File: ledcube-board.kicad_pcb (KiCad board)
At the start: 4 copper layers, 181 parts, among them J1 Conn_01x02, J10 molex_53261-0871, J11 104031-0811, J12 molex_53261-0871, J2 molex_53261-0871, J3 molex_53261-0871, J4 molex_53261-0871, J5 molex_53261-0871, J6 molex_53261-0871, J7 molex_53261-0871, J8 molex_53261-0871, J9 molex_53261-0871, Q1 Q_NMOS_GDSD, Q2 Q_NMOS_GDSD, Q3 Q_NMOS_GDSD, Q4 Q_NMOS_GDSD, Q5 Q_NMOS_GDSD, Q6 Q_NMOS_GDSD, Q7 Q_NMOS_GDSD, Q8 Q_NMOS_GDSD, U1 LM1085IS-12, U10 ESP32-DEVKITC-32D, U11 IP4220CZ6, U12 IP4220CZ6, U13 XC9572XL-VQ64, U14 SN74LVCC3245APWR, U15 SN74LVCC3245APWR, U2 STP08CP05MTR, U3 STP08CP05MTR, U4 STP08CP05MTR, U5 STP08CP05MTR, U6 STP08CP05MTR, U7 STP08CP05MTR, U8 STP08CP05MTR, U9 STP08CP05MTR, X1 ASE-40MHz, X2 ASE-25MHz

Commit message: PCB: Placement @ 95%
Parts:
- C11, C12, C13, C14, J10, J12, J7, J8, J9, R48, R49, R50, R51, R52, R53, R54, R55, R56, R57, R58, R59, R60, R61, R62, R63, R64, R65, R66, R67, R68, R69, R70, R71, R72, R73, R74, R75, R76, R77, R78, R79, R94, R95, R96, R97, U6, U7, U8, U9: moved to B.Cu
- moved C31 299.1 mm to (-16.5, 148.2), turned to 180 degrees
- moved C20 296.7 mm to (-9.00, 163.2), turned to 270 degrees
- moved C28 282.5 mm to (-12.0, 163.2), turned to 270 degrees
- moved C26 278.0 mm to (-16.5, 145.2), turned to 180 degrees
- moved C25 276.3 mm to (4.25, 159.5), turned to 270 degrees
- moved C30 274.2 mm to (7.25, 159.5), turned to 270 degrees
- moved C29 263.8 mm to (8.00, 140.8), turned to 90 degrees
- moved C27 261.4 mm to (11.0, 140.8), turned to 90 degrees
- moved J12 160.2 mm to (115.0, 98.0), turned to 180 degrees
- moved R94 154.5 mm to (111.0, 84.8), turned to 270 degrees
- moved R95 153.0 mm to (113.9, 84.8), turned to 270 degrees
- moved R96 151.5 mm to (116.8, 84.8), turned to 270 degrees
- moved R97 150.1 mm to (119.8, 84.8), turned to 270 degrees
- moved U15 142.0 mm to (-3.50, 131.2), turned to 180 degrees
- moved R83 139.3 mm to (84.5, 6.75)
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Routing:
- net /pl.sch/VCC_3V3: track 0.00 -> 14.8 mm
- net /pl.sch/GPIO3: track 0.00 -> 14.1 mm
- net /pl.sch/GPIO2: track 0.00 -> 12.2 mm
- net /pl.sch/GPIO1: track 0.00 -> 10.4 mm
- net /pl.sch/GPIO0: track 0.00 -> 9.52 mm
- net /pl.sch/CLK_25M: track 8.07 -> 11.0 mm
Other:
- board outline added: 100.8 x 86.8 mm

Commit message: Change footprint from 0805 to 1206 of resistors that connect I2C_3V3 and SD_3V3 to source
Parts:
- R92, R93: footprint Resistor_SMD:R_0603_1608Metric_Pad1.05x0.95mm_HandSolder -> Resistor_SMD:R_1206_3216Metric_Pad1.30x1.75mm_HandSolder
- moved R14 243.8 mm to (-16.2, 127.0), turned to 180 degrees
- moved R13 242.9 mm to (-16.2, 133.5)
- moved R15 241.6 mm to (-16.2, 130.2), turned to 180 degrees
- moved R92 136.9 mm to (77.8, 55.2)
- moved R81 134.7 mm to (75.8, 66.8), turned to 180 degrees
- moved C17 132.6 mm to (87.6, 50.0), turned to 270 degrees
- moved R87 131.2 mm to (79.5, 65.9), turned to 270 degrees
- moved R82 129.0 mm to (75.8, 69.2), turned to 180 degrees
- moved C15 128.0 mm to (87.7, 42.2)
- moved C16 126.0 mm to (84.5, 50.0), turned to 270 degrees
- moved R85 120.9 mm to (79.5, 70.2), turned to 90 degrees
- moved R93 119.1 mm to (77.8, 59.0)
- moved R88 112.0 mm to (88.8, 35.8), turned to 270 degrees
- moved U12 100.5 mm to (3.00, 101.5)
- moved U11 94.3 mm to (8.25, 101.5)
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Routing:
- net /ps.sch/SD_CD: track 0.00 -> 14.0 mm
- net /layer_led_mux.sch/CLK: track 0.00 -> 12.2 mm
- net /pl.sch/DATA_LE_5V5: track 0.00 -> 9.67 mm
- net /pl.sch/~DATA_OE_5V5: track 0.00 -> 9.11 mm
- net /pl.sch/I2C_SDA: track 0.00 -> 2.89 mm
- net /pl.sch/I2C_SCL: track 0.00 -> 2.83 mm

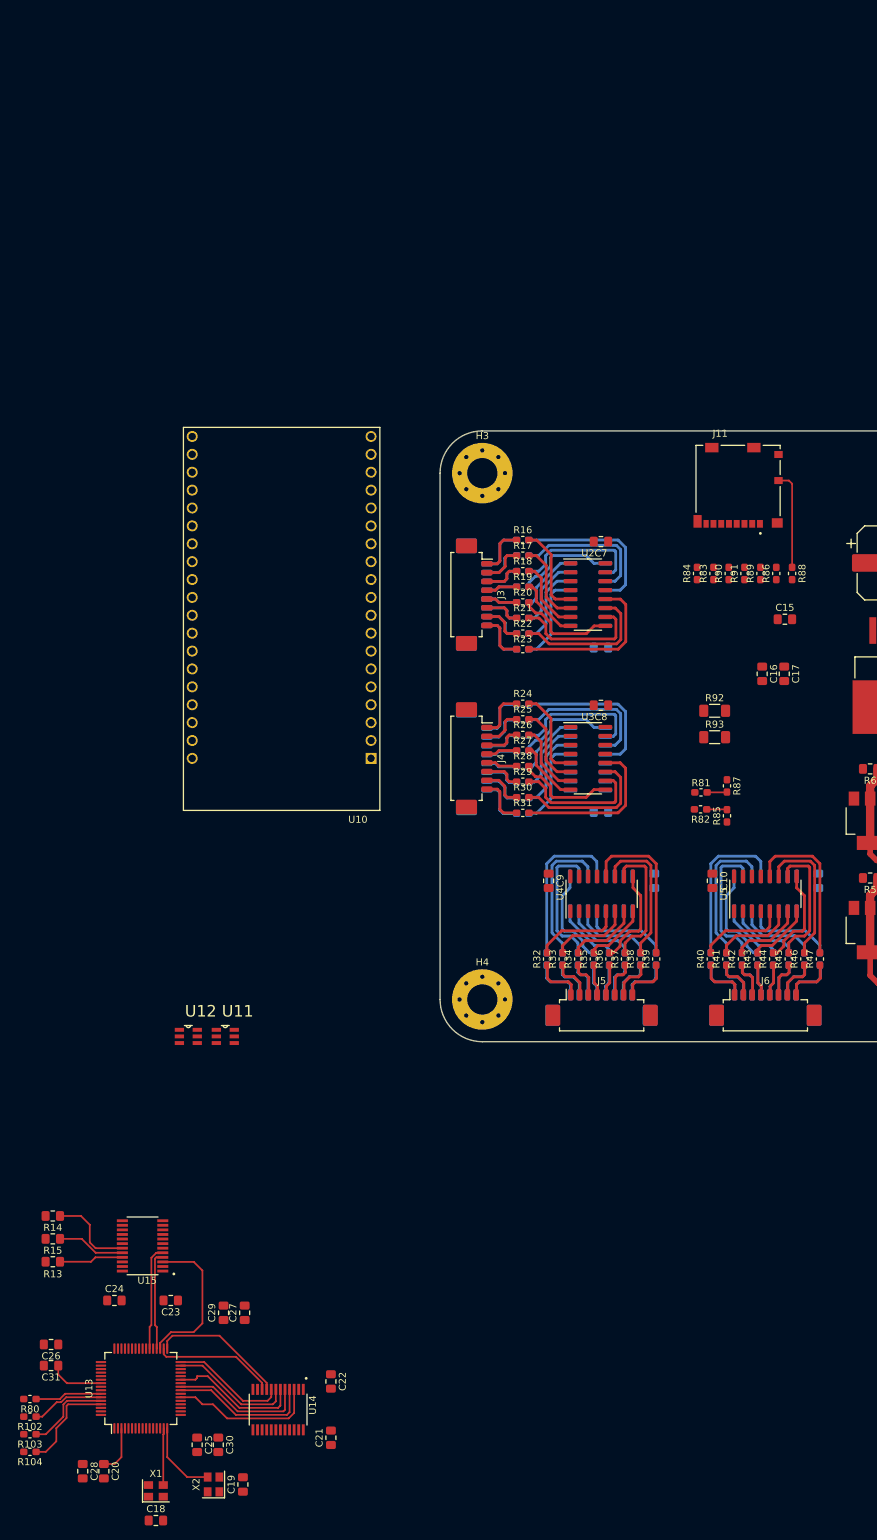
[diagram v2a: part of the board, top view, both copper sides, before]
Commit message: Chnage line for SD protection
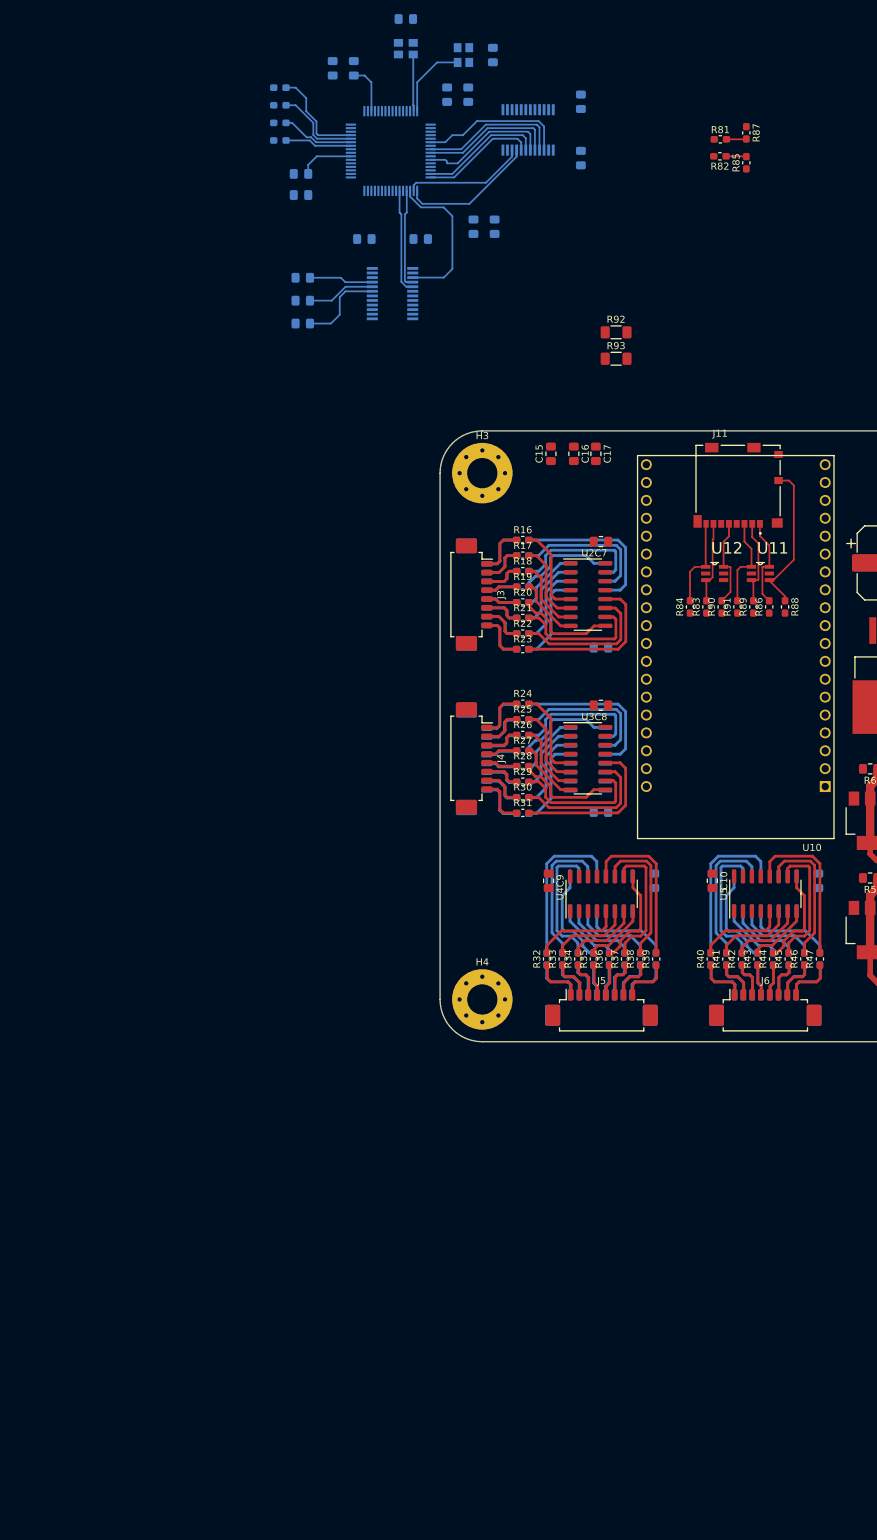
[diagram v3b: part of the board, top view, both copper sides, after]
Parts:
- C18, C19, C20, C21, C22, C23, C24, C25, C26, C27, C28, C29, C30, C31, R102, R103, R104, R13, R14, R15, R80, U13, U14, U15, X1, X2: moved to B.Cu
- moved C18 216.2 mm to (33.9, -43.0)
- moved X1 207.9 mm to (33.9, -38.8)
- moved C19 206.1 mm to (46.2, -37.9), turned to 270 degrees
- moved X2 206.1 mm to (42.1, -37.9), turned to 270 degrees
- moved C20 202.4 mm to (26.5, -36.0), turned to 90 degrees
- moved C28 202.4 mm to (23.5, -36.0), turned to 90 degrees
- moved R104 197.0 mm to (16.0, -33.2)
- moved C25 195.0 mm to (39.8, -32.2), turned to 90 degrees
- moved C30 195.0 mm to (42.8, -32.2), turned to 90 degrees
- moved C21 193.0 mm to (58.8, -31.2), turned to 270 degrees
- moved R103 192.1 mm to (16.0, -30.8)
- moved R102 187.1 mm to (16.0, -28.2)
- moved U14 185.2 mm to (51.2, -27.2), turned to 90 degrees
- moved R80 182.2 mm to (16.0, -25.8)
- moved U13 179.3 mm to (31.8, -24.2), turned to 270 degrees
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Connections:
- U11 pad 1: /ps.sch/SD_DAT3 -> /ps.sch/SD_CMD
- U11 pad 3: /ps.sch/SD_DAT2 -> /ps.sch/SD_DAT3
- U11 pad 6: /ps.sch/SD_CMD -> /ps.sch/SD_DAT2
- U12 pad 6: Net-(U12-Pad6) -> /ps.sch/SD_CLK
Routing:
- net /ps.sch/SD_CMD: track 0.00 -> 13.1 mm
- net /ps.sch/SD_DAT2: track 0.00 -> 12.8 mm
- net /ps.sch/SD_DAT1: track 0.00 -> 12.8 mm
- net /ps.sch/SD_CLK: track 0.00 -> 12.7 mm
- net /ps.sch/SD_DAT3: track 0.00 -> 12.3 mm
- net /ps.sch/SD_DAT0: track 0.00 -> 11.8 mm
- net /ps.sch/SD_CD: track 14.0 -> 21.6 mm

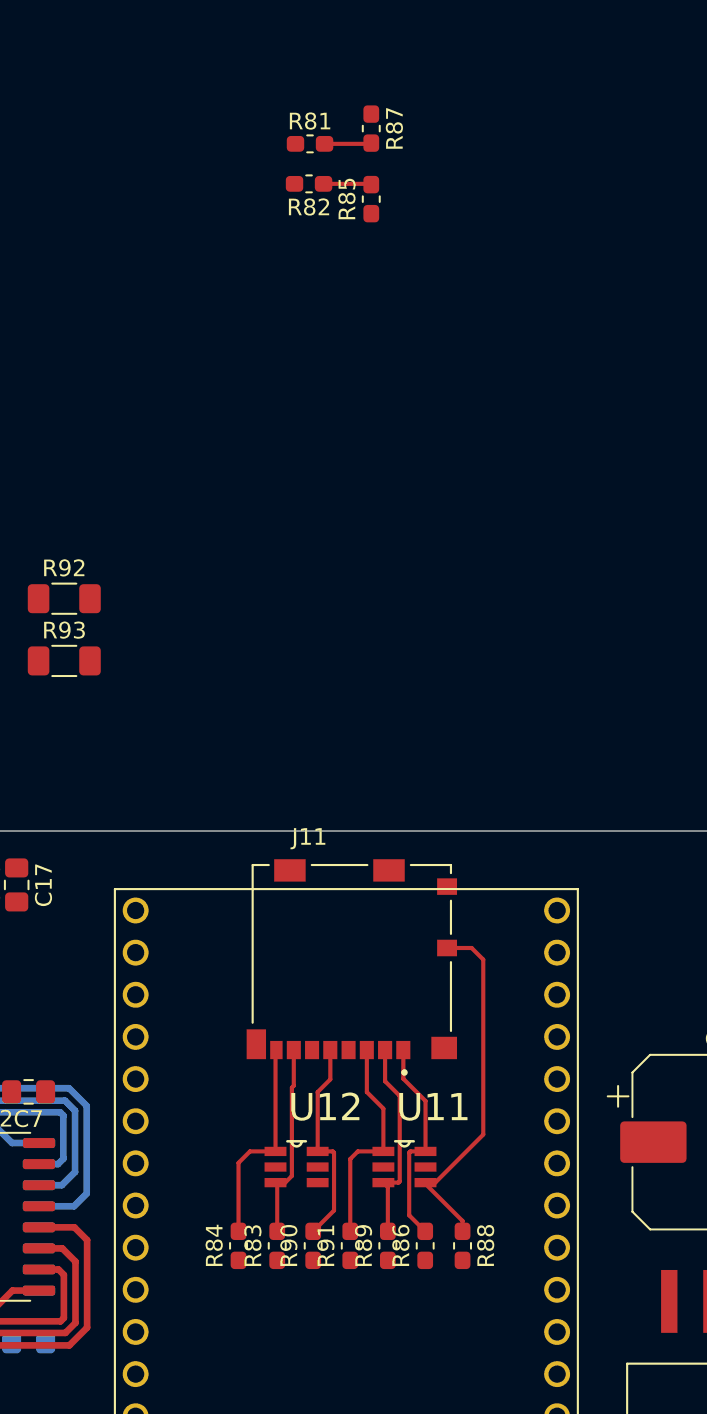
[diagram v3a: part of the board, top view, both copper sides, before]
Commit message: PCB: Placement @ 98%
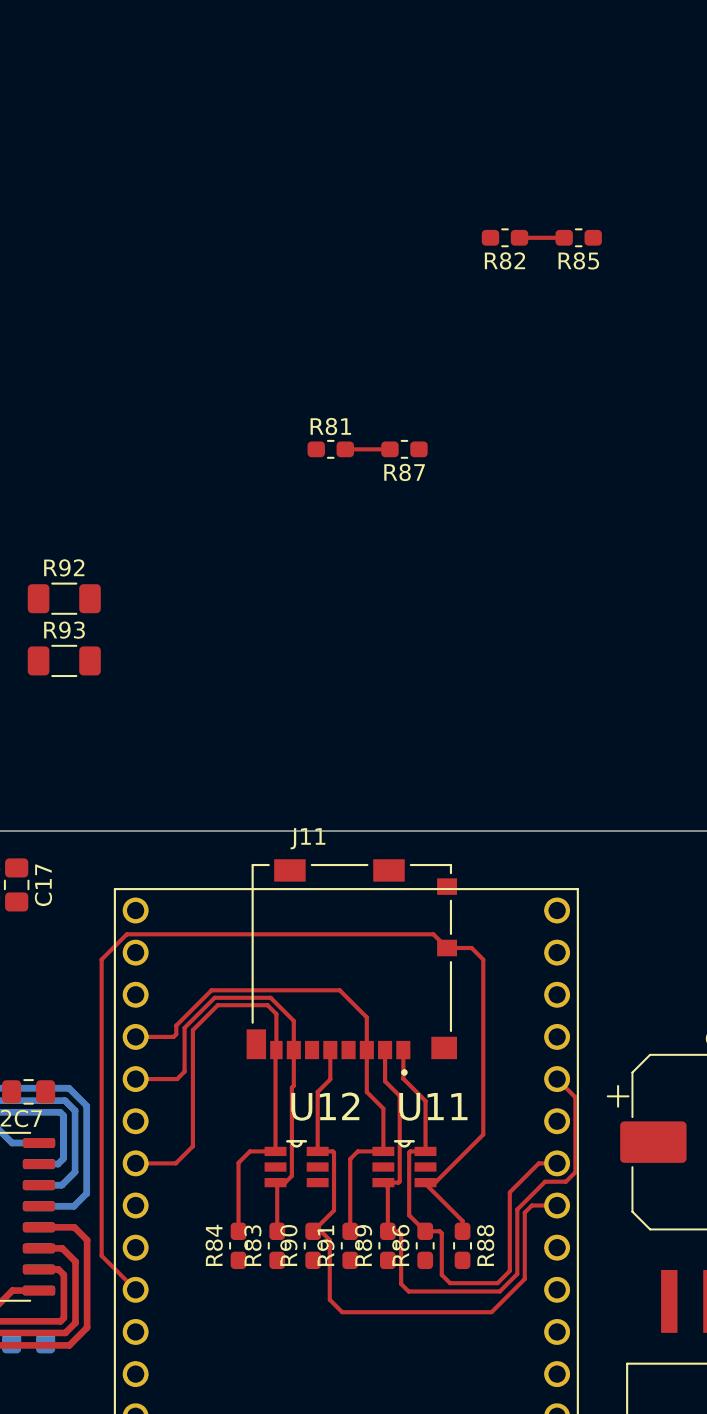
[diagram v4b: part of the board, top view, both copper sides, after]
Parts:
- moved R87 19.4 mm to (84.2, -7.50), turned to 180 degrees
- moved R81 18.5 mm to (79.8, -7.50)
- moved R85 12.7 mm to (94.8, -20.2), turned to 180 degrees
- moved R82 12.2 mm to (90.3, -20.2)
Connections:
- U10 pad 29: Net-(U10-Pad29) -> /ps.sch/SD_CD
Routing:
- net /ps.sch/SD_CD: track 21.6 -> 64.1 mm
- net /ps.sch/SD_DAT3: track 12.3 -> 38.2 mm
- net /ps.sch/SD_CLK: track 12.7 -> 36.5 mm
- net /ps.sch/SD_DAT1: track 12.8 -> 31.7 mm
- net /ps.sch/SD_CMD: track 13.1 -> 31.1 mm
- net /ps.sch/SD_DAT2: track 12.8 -> 29.4 mm
- net /ps.sch/SD_DAT0: track 11.8 -> 27.2 mm

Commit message: PCB: Place all components
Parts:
- R102, R103, R104, R80: footprint Resistor_SMD:R_0603_1608Metric_Pad1.05x0.95mm_HandSolder -> Resistor_SMD:R_0603_1608Metric_Pad0.98x0.95mm_HandSolder
- moved C18 119.5 mm to (69.5, 71.1), turned to 90 degrees
- moved C20 117.0 mm to (90.2, 62.1), turned to 0 degrees
- moved X1 116.9 mm to (73.7, 71.1), turned to 90 degrees
- moved C28 116.2 mm to (90.2, 59.1), turned to 0 degrees
- moved R103 115.1 mm to (90.3, 57.2), turned to 0 degrees
- moved R104 113.9 mm to (89.5, 53.8), turned to 0 degrees
- moved X2 108.8 mm to (71.4, 66.9), turned to 0 degrees
- moved R102 105.9 mm to (89.1, 48.4), turned to 0 degrees
- moved R80 105.9 mm to (89.1, 50.8), turned to 0 degrees
- moved C19 103.7 mm to (71.4, 62.8), turned to 0 degrees
- moved U13 97.2 mm to (81.1, 59.5), turned to 90 degrees
- moved C27 93.8 mm to (86.2, 71.5)
- moved C29 93.8 mm to (83.2, 71.5)
- moved C26 92.5 mm to (71.4, 58.2)
- moved C31 92.5 mm to (71.4, 55.2)
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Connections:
- R102 pad 2: /ps.sch/ESP_GPIO3 -> /ps.sch/ESP_GPIO1
- R103 pad 2: /ps.sch/ESP_GPIO0 -> /ps.sch/ESP_GPIO2
- R104 pad 2: /ps.sch/ESP_GPIO1 -> /ps.sch/ESP_GPIO3
- R80 pad 2: /ps.sch/ESP_GPIO2 -> /ps.sch/ESP_GPIO0
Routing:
- net /pl.sch/DATA_LE_5V5: track 9.67 -> 162.5 mm, vias 0 -> 9
- net /layer_led_mux.sch/CLK: track 12.2 -> 153.2 mm, vias 0 -> 7
- net /pl.sch/~DATA_OE_5V5: track 9.11 -> 135.1 mm, vias 0 -> 7
- net /DATA_LED3: track 0.00 -> 100.5 mm, vias 0 -> 1
- net /DATA_LED7: track 0.00 -> 82.0 mm, vias 0 -> 6
- net /DATA_LED4: track 0.00 -> 80.6 mm, vias 0 -> 1
- net /LAYER_SEL7: track 0.00 -> 80.2 mm, vias 0 -> 3
- net /DATA_LED6: track 0.00 -> 77.3 mm, vias 0 -> 2
- net /pl.sch/LED_R: track 0.00 -> 75.6 mm, vias 0 -> 1
- net /pl.sch/LED_G: track 0.00 -> 73.1 mm, vias 0 -> 3
- net /LAYER_SEL5: track 0.00 -> 71.8 mm, vias 0 -> 3
- net /pl.sch/LED_O1: track 0.00 -> 70.5 mm, vias 0 -> 3
- net /pl.sch/DATA_LE_3V3: track 14.1 -> 82.3 mm
- net /pl.sch/LED_O2: track 0.00 -> 65.3 mm, vias 0 -> 3
- net /LAYER_SEL8: track 0.00 -> 62.6 mm, vias 0 -> 1
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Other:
- net class layer_selection: clearance 0.3 -> 0.2
- net class led_pwr: clearance 0.3 -> 0.2
